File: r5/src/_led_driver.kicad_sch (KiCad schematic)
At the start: 7 parts, among them J16 FH12A-20S-0.5SH, Q22 NX3008NBKW, U9 PCF8574PW

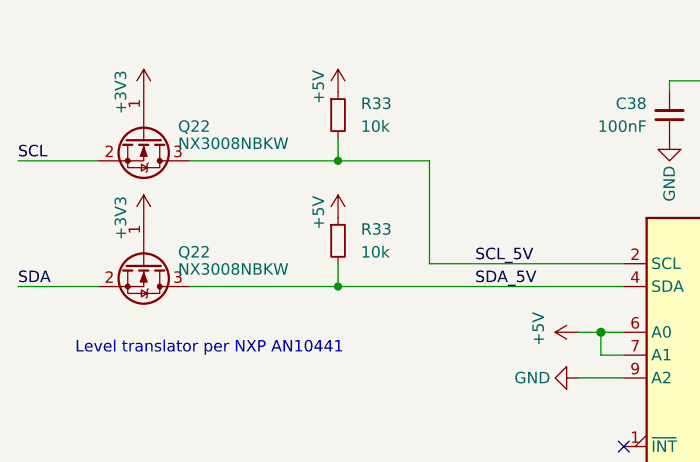
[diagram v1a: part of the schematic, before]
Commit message: Update to new Kicad nightly - file format update
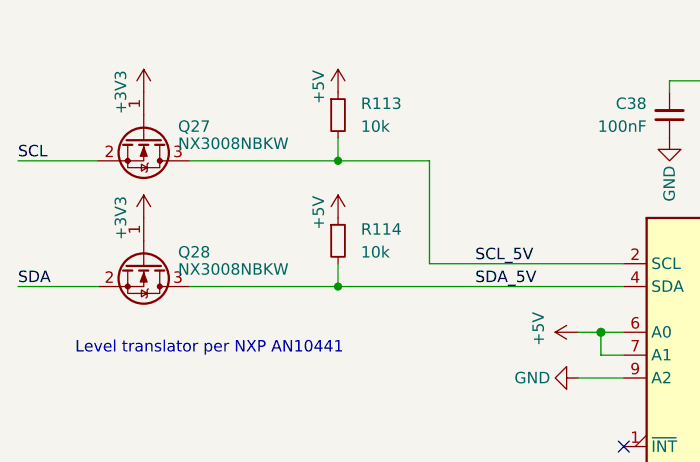
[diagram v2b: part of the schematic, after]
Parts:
- renumbered Q22 to Q27, Q22 to Q28, R33 to R113, R33 to R114
